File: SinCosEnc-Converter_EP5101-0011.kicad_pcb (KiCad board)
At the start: 2 copper layers, 88.3 x 61.8 mm, 83 parts, among them J1 Conn_01x05_Pin, J2 Conn_02x05_Top_Bottom, SW1 SW_RCLK, SW2 SW_SG1, SW3 SW_SG0, SW4 SW_ROT, SW5 SW_SF1, SW6 SW_SF0, U1 iC-NV, U2 AM26LS31CDR, U3 AP22652AW6-7, X2 D-SUB-DR-15PCG-AB

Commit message: v0.9.2 finished, board routed
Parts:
- removed D1: 1N4007, Diode_SMD:D_SMA
- added JP8: DiagRPP, Jumper:SolderJumper-3_P1.3mm_Bridged12_RoundedPad1.0x1.5mm, F.Cu at (123.4, 100.2)
- added U4: LM66100DCKR, easyeda2kicad:SC-70-6_L2.0-W1.3-P0.65-LS2.1-BL, F.Cu at (126.6, 105.9)
- RV1_TP1, RV1_TP2: moved to B.Cu
- moved SW5 79.0 mm to (75.8, 70.3)
- moved R8 72.1 mm to (79.6, 110.3)
- moved R6 64.2 mm to (79.6, 101.4)
- moved SW4 61.8 mm to (75.8, 58.9)
- moved SW6 61.8 mm to (75.8, 81.8)
- moved R3 59.7 mm to (103.1, 69.1), turned to 90 degrees
- moved R9 54.3 mm to (93.1, 92.6), turned to 90 degrees
- moved RV1_TP2 51.1 mm to (83.5, 56.4), turned to 180 degrees
- moved C5 48.4 mm to (98.8, 69.1)
- moved C4 47.2 mm to (98.8, 85.6)
- moved C6 45.0 mm to (96.1, 98.3), turned to -90 degrees
- moved R11 45.0 mm to (124.9, 69.1), turned to 90 degrees
- moved Ch2_RS4 44.1 mm to (117.0, 80.5)
- moved Ch3_RS4 44.0 mm to (125.9, 80.6)
- moved Ch2_CS4 42.9 mm to (116.4, 83.1), turned to 0 degrees
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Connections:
- FB1 pad 1: CON_VCC -> Net-(U4-VOUT)
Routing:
- net +5V: track 0.00 -> 266.1 mm, vias 0 -> 2
- net CON_~{ERR}: track 0.00 -> 143.9 mm, vias 0 -> 2
- net +5V_Sensor: track 0.00 -> 109.5 mm, vias 0 -> 4
- net GND: track 0.00 -> 108.2 mm, vias 0 -> 104
- net iC-VREF: track 0.00 -> 74.3 mm, vias 0 -> 5
- net Sensor_IN_ZERO+: track 0.00 -> 72.6 mm, vias 0 -> 2
- net Sensor_IN_SIN+: track 0.00 -> 72.6 mm, vias 0 -> 2
- net Sensor_IN_COS+: track 0.00 -> 72.5 mm, vias 0 -> 2
- net Sensor_IN_COS-: track 0.00 -> 72.5 mm, vias 0 -> 2
- net Sensor_IN_ZERO-: track 0.00 -> 72.5 mm, vias 0 -> 2
- net Sensor_IN_SIN-: track 0.00 -> 72.5 mm, vias 0 -> 2
- net iC-ROT: track 0.00 -> 64.8 mm, vias 0 -> 2
- net Net-(SW1-B): track 0.00 -> 64.4 mm, vias 0 -> 2
- net CON_VCC: track 0.00 -> 63.4 mm
- net DifSig_A+: track 0.00 -> 61.3 mm
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- added copper zone on B.Cu, net GND
- added copper zone on F.Cu, net GND
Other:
- board size 88.3 x 61.8 mm -> 88 x 61.8 mm
- board text added: "Channel 3-ZER"
- board text added: "RS4"
- board text removed: "Channel 3-ZERO"

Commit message: first theoretical working PCB finished (v0.9.3)
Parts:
- added G***: LOGO, LOGO, B.Cu at (86.8, 61.1)
- added G***: LOGO, LOGO, B.Cu at (145.6, 84.8)
- added R1: 180k, Resistor_SMD:R_0603_1608Metric, F.Cu at (150.7, 110.8)
- added REF**: LOGO_PedPEx, CostumLibrary:LOGO_PedPEx, B.Cu at (132.1, 66.5)
- R2: value 180k -> 0
- R4: value 0 -> 10k
- moved R2 8.20 mm to (144.1, 105.9)
- moved R4 3.50 mm to (147.6, 106.5), turned to 0 degrees
- moved JP7 1.91 mm to (147.6, 104.0)
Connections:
- R2 pad 1: Net-(U3-ILIM) -> +5V_Sensor
- R2 pad 2: GND -> +5V
- R4 pad 1: +5V_Sensor -> +5V
- R4 pad 2: +5V -> CON_~{ERR}
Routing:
- net +5V: track 266.1 -> 272.9 mm
- net CON_~{ERR}: track 143.9 -> 149.3 mm
- net +5V_Sensor: track 109.5 -> 114.8 mm
- net iC-SF1: track 56.7 -> 55.2 mm
- net iC-SF0: track 46.1 -> 44.8 mm
- net GND: track 108.2 -> 109.1 mm
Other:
- board text added: "${ISSUE_DATE} ©PedPEx v${REVISION}"
- board text added: "-> 11µA_{pp} all NOT closed high | open low | low low open open high 7.125 | 4 IPF: 5"
- board text added: "1 SIN+"
- board text added: "10 GND"
- board text added: "2 SIN-"
- board text added: "3 5V"
- board text added: "4 GND"
- board text added: "5 COS+"
- board text added: "6 COS-"
- board text added: "7 ZERO+"
- board text added: "8 ZERO-"
- board text added: "9 GND"
- board text added: "CON_Gate"
- board text added: "CON_Latch"
- board text added: "CON_VCC"
- board text added: "CON_~{ERR}"
- board text added: "Configs: -> 1V_{pp} ChX_JP1 all closed SW_SG0: open SW_SG1: low SW_ROT: low SW_SF0: open SW_SF1: open SW_RCLK: high => Gain: 8 IPF: 5"
- board text added: "GND"
- board text added: "Green: 5V sensor Yellow: Fault"
- board text added: "PinOut on RJ45: Pin1 - Pin8 identical Pin9 & 10 omitted"
- board text added: "Put your multimeter in Ohmski-Mode here to measure RV1"
- board text added: "RCLK"
- board text added: "ROT"
- board text added: "SF0"
- board text added: "SF1"
- board text added: "SG0"
- board text added: "SG1"
- board text added: "VCC"
- board text added: "high"
- board text added: "low"
- board text added: "open"
- board text added: "pot"

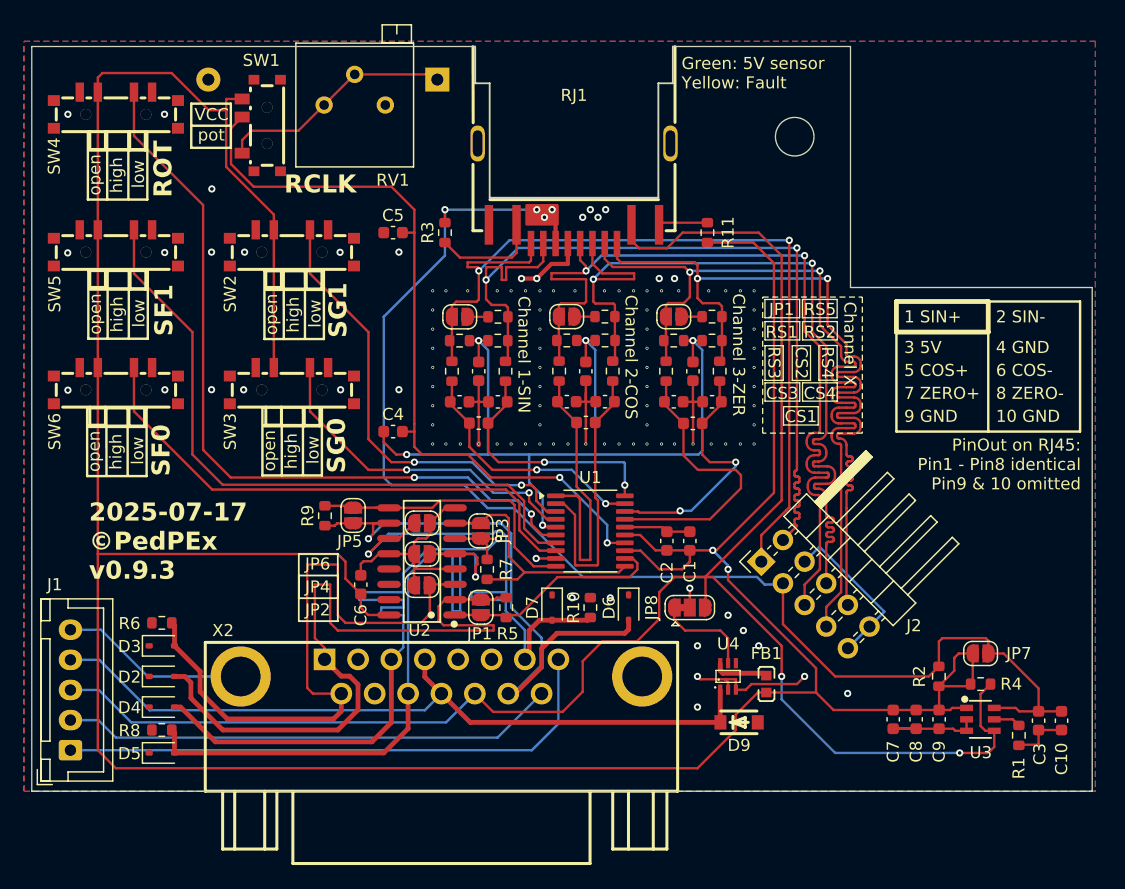
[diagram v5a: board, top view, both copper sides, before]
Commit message: cleaned up board layout -> v0.9.5 from v0.9.5 to v0.9.5 just minor optical improvements were done
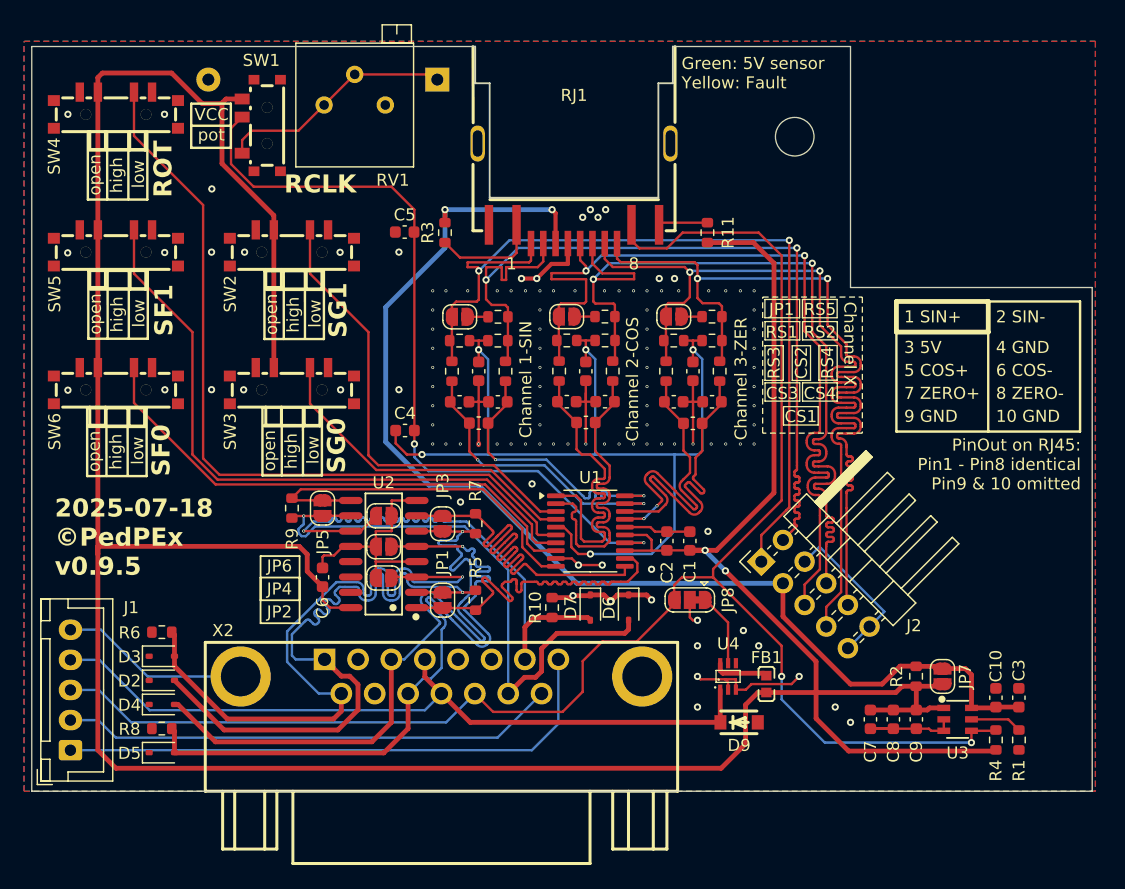
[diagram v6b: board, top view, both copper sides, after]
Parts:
- moved C10 5.77 mm to (148.8, 107.7), turned to -90 degrees
- moved R4 4.81 mm to (148.8, 111.2), turned to 90 degrees
- moved R7 3.91 mm to (105.6, 93.2), turned to 90 degrees
- moved JP7 3.69 mm to (144.4, 105.9), turned to -90 degrees
- moved C6 3.23 mm to (92.9, 97.7)
- moved JP2 3.23 mm to (98.0, 97.7)
- moved JP4 3.23 mm to (98.0, 95.1)
- moved JP6 3.23 mm to (98.0, 92.6)
- moved U2 3.23 mm to (98.0, 95.7)
- moved JP3 3.23 mm to (102.9, 93.2)
- moved JP1 3.23 mm to (102.9, 99.6)
- moved D7 3.17 mm to (115.2, 100.2)
- moved R10 3.17 mm to (112.0, 100.2)
- moved R9 2.81 mm to (90.4, 91.9)
- moved JP5 2.61 mm to (92.9, 91.9)
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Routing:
- net TTL_Sig_B: track 21.8 -> 38.6 mm
- net +5V_Sensor: track 114.8 -> 100.4 mm, vias 4 -> 2
- net TTL_Sig_A: track 18.4 -> 30.6 mm
- net CON_~{ERR}: track 149.3 -> 140.4 mm
- net iC-VREF: track 74.3 -> 82.6 mm
- net GND: track 109.1 -> 116.9 mm, vias 104 -> 110
- net TTL_Sig_C: track 23.8 -> 30.9 mm
- net iC-ZERO-: track 21.0 -> 27.4 mm, vias 2 -> 0
- net DifSig_C-: track 41.9 -> 47.9 mm
- net +5V: track 272.9 -> 278.5 mm
- net DifSig_B-: track 58.4 -> 62.8 mm
- net DifSig_A-: track 54.1 -> 58.1 mm, vias 0 -> 1
- net DifSig_B+: track 58.2 -> 61.8 mm
- net iC-SIN+: track 21.2 -> 24.6 mm
- net iC-SIN-: track 21.2 -> 24.5 mm
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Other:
- board text added: "1"
- board text added: "8"

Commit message: version 0.9.6 finished
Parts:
- removed the J1 at (72.0, 112.0)
- removed JP8: DiagRPP, Jumper:SolderJumper-3_P1.3mm_Bridged12_RoundedPad1.0x1.5mm
- added C11: 0.1u, Capacitor_SMD:C_0603_1608Metric, F.Cu at (151.2, 107.7)
- added C12: 47u, Capacitor_SMD:C_1206_3216Metric, F.Cu at (148.8, 107.0)
- added C13: 4n7, Capacitor_SMD:C_1808_4520Metric, F.Cu at (83.6, 94.6)
- added D1: SMAJ5.0CA, Diode_SMD:D_SMA, F.Cu at (127.7, 110.3)
- added D10: ESD401DPYR, CostumLibrary:Texas_DPY0002A_0.6x1mm_P0.65mm, F.Cu at (123.4, 98.7)
- added D11: ESD401DPYR, CostumLibrary:Texas_DPY0002A_0.6x1mm_P0.65mm, F.Cu at (121.5, 98.7)
- added D12: ESD401DPYR, CostumLibrary:Texas_DPY0002A_0.6x1mm_P0.65mm, F.Cu at (88.4, 91.9)
- added D8: LED RED, LED_SMD:LED_0603_1608Metric, F.Cu at (104.2, 64.0)
- added R12: 1M, Resistor_SMD:R_2010_5025Metric, F.Cu at (83.8, 97.6)
- C10: value 0.1u -> 47u; footprint Capacitor_SMD:C_0603_1608Metric -> Capacitor_SMD:C_1206_3216Metric
- D9: value SMF5.0A -> LED GREEN; footprint easyeda2kicad:SOD-123F_L2.8-W1.8-LS3.7-RD -> LED_SMD:LED_0603_1608Metric
- R1: value 180k -> 215k
- RJ1: value RC01812 -> 6339160-1; footprint easyeda2kicad:RJ45-TH_RC01812 -> easyeda2kicad:RJ45-SMD_6339160-1
- RV1: value 500k -> 50k; footprint Potentiometer_THT:Potentiometer_Bourns_3296P_Horizontal -> Potentiometer_THT:Potentiometer_Bourns_3266X_Horizontal
- moved D9 52.2 mm to (102.4, 64.0), turned to -90 degrees
- moved R11 20.7 mm to (104.2, 69.1)
- moved C5 13.4 mm to (99.8, 82.4)
- moved C10 6.68 mm to (142.3, 109.2), turned to 90 degrees
- moved RV1 4.86 mm to (94.1, 61.2)
- moved G*** 2.94 mm to (83.9, 60.4)
- moved RV1_TP1 2.61 mm to (99.9, 55.8)
- moved RV1_TP2 2.61 mm to (80.9, 55.8)
- moved C3 2.41 mm to (153.1, 107.7)
- moved C7 2.29 mm to (136.1, 109.6)
- moved C8 2.29 mm to (138.0, 109.6)
- moved C9 2.29 mm to (139.9, 109.6)
- moved D2 2.16 mm to (77.5, 106.2)
- moved D3 2.16 mm to (77.5, 104.2)
- moved D4 2.16 mm to (77.5, 108.2)
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- renumbered J2 to J1
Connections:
- C10 pad 2: +5V_Sensor -> +5V
- D9 pad 1: CON_VCC -> GND
- D9 pad 2: GND -> Net-(D9-A)
- FB1 pad 1: Net-(U4-VOUT) -> +5V
- FB1 pad 2: +5V -> Net-(U4-VOUT)
- J1 pad 10: GND -> GNDS
- J1 pad 3: +5V_Sensor -> Sensor_IN_COS+
- J1 pad 4: GND -> Sensor_IN_COS-
- J1 pad 5: Sensor_IN_COS+ -> Sensor_IN_ZERO+
- J1 pad 6: Sensor_IN_COS- -> Sensor_IN_ZERO-
- J1 pad 7: Sensor_IN_ZERO+ -> GND
- J1 pad 8: Sensor_IN_ZERO- -> GNDS
- J1 pad 9: GND -> +5V_Sensor
- R11 pad 2: Net-(RJ1-Y+) -> Net-(D8-A)
- R3 pad 1: Net-(RJ1-G+) -> Net-(D9-A)
- RJ1 pad 10: Net-(RJ1-G+) -> GNDS
- RJ1 pad 4: GND -> Sensor_IN_COS+
- RJ1 pad 5: Sensor_IN_COS+ -> Sensor_IN_COS-
- RJ1 pad 6: Sensor_IN_COS- -> GND
- RJ1 pad 9: GND -> GNDS
- U4 pad 5: Net-(JP8-A) -> CON_~{ERR}
- X2 pad 15: CON_Gate -> unconnected-(X2-Pad15)
- X2 pad 16: GND -> GNDS
- X2 pad 17: GND -> GNDS
- X2 pad 8: CON_Latch -> unconnected-(X2-Pad8)
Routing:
- net GNDS: track 0.00 -> 160.6 mm, vias 0 -> 5
- net CON_Latch: track 46.7 -> 0.00 mm
- net CON_Gate: track 41.2 -> 0.00 mm
- net CON_VCC: track 63.4 -> 31.0 mm
- net GND: track 116.9 -> 146.0 mm, vias 110 -> 125
- net CON_~{ERR}: track 140.4 -> 124.2 mm
- net +5V: track 278.5 -> 264.0 mm
- net Net-(RJ1-G+): track 8.94 -> 0.00 mm
- net TTL_Sig_A: track 30.6 -> 37.7 mm
- net Net-(JP8-A): track 6.03 -> 0.00 mm
- net Net-(RJ1-Y+): track 4.08 -> 0.00 mm
- net +5V_Sensor: track 100.4 -> 96.6 mm, vias 2 -> 1
- net Sensor_IN_SIN-: track 72.1 -> 75.6 mm
- net Net-(D9-A): track 0.00 -> 3.47 mm
- net Net-(D8-A): track 0.00 -> 3.47 mm
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- added copper zone on F.Cu, net GNDS
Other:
- outline, holes or cut-outs redrawn
- board text added: "10 Shield"
- board text added: "2: SIN- 4: COS+ 6: GND 8: ZER-"
- board text added: "3 COS+"
- board text added: "4 COS-"
- board text added: "5 ZERO+"
- board text added: "6 ZERO-"
- board text added: "7 GND"
- board text added: "8 Shield"
- board text added: "9 5V"
- board text added: "Green: 5V PWR Red: Fault"
- board text added: "PinOut on RJ45: 1: SIN+ 3: 5V 5: COS- 7: ZER+"
- board text added: "Put your multimeter in Ohmski-mode here to measure RV1 (SW1 in VCC position!)"
- board text removed: "10 GND"
- board text removed: "3 5V"
- board text removed: "4 GND"
- board text removed: "5 COS+"
- board text removed: "6 COS-"
- board text removed: "7 ZERO+"
- board text removed: "8 ZERO-"
- board text removed: "9 GND"
- board text removed: "CON_Gate"
- board text removed: "CON_Latch"
- board text removed: "CON_VCC"
- board text removed: "CON_~{ERR}"
- board text removed: "GND"
- board text removed: "Green: 5V sensor Yellow: Fault"
- board text removed: "PinOut on RJ45: Pin1 - Pin8 identical Pin9 & 10 omitted"
- board text removed: "Put your multimeter in Ohmski-Mode here to measure RV1"
